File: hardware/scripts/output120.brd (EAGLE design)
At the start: 100 x 80 mm, 378 parts

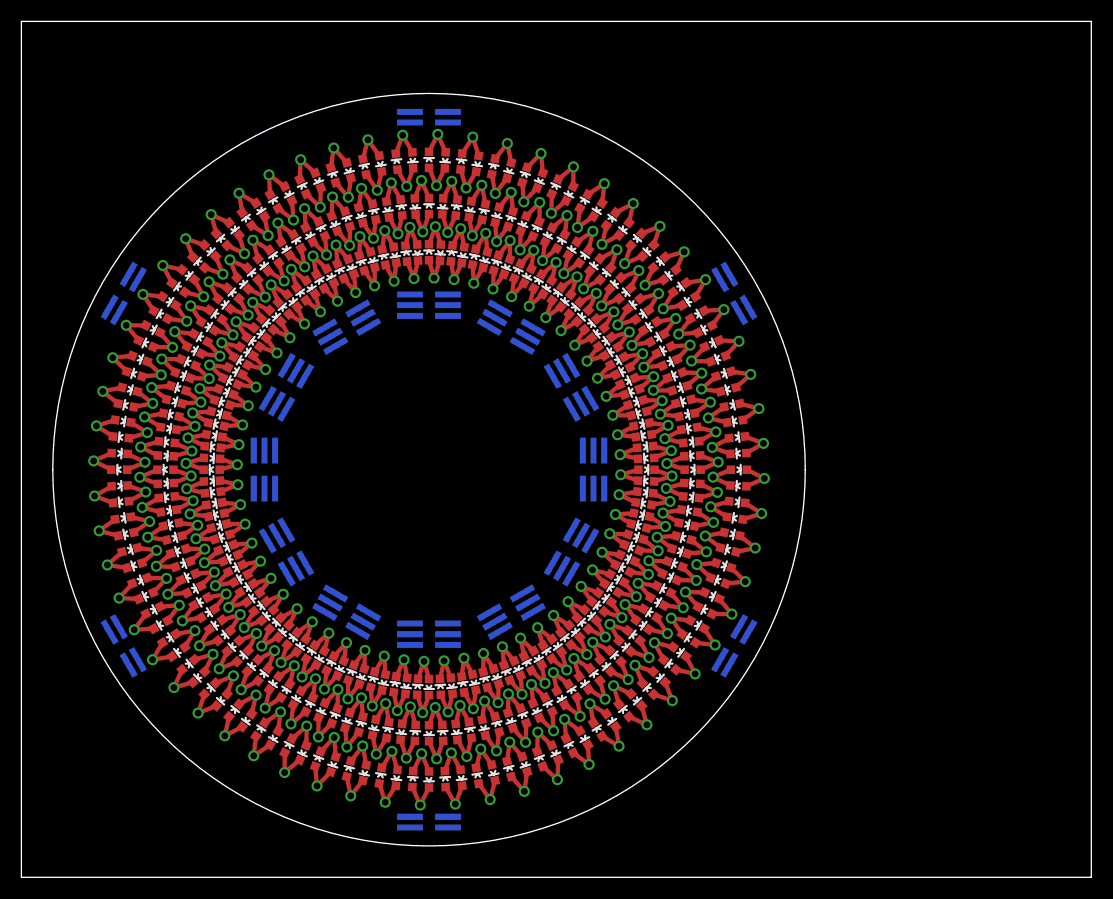
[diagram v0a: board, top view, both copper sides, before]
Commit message: More cleanup and reorganization of old attempts
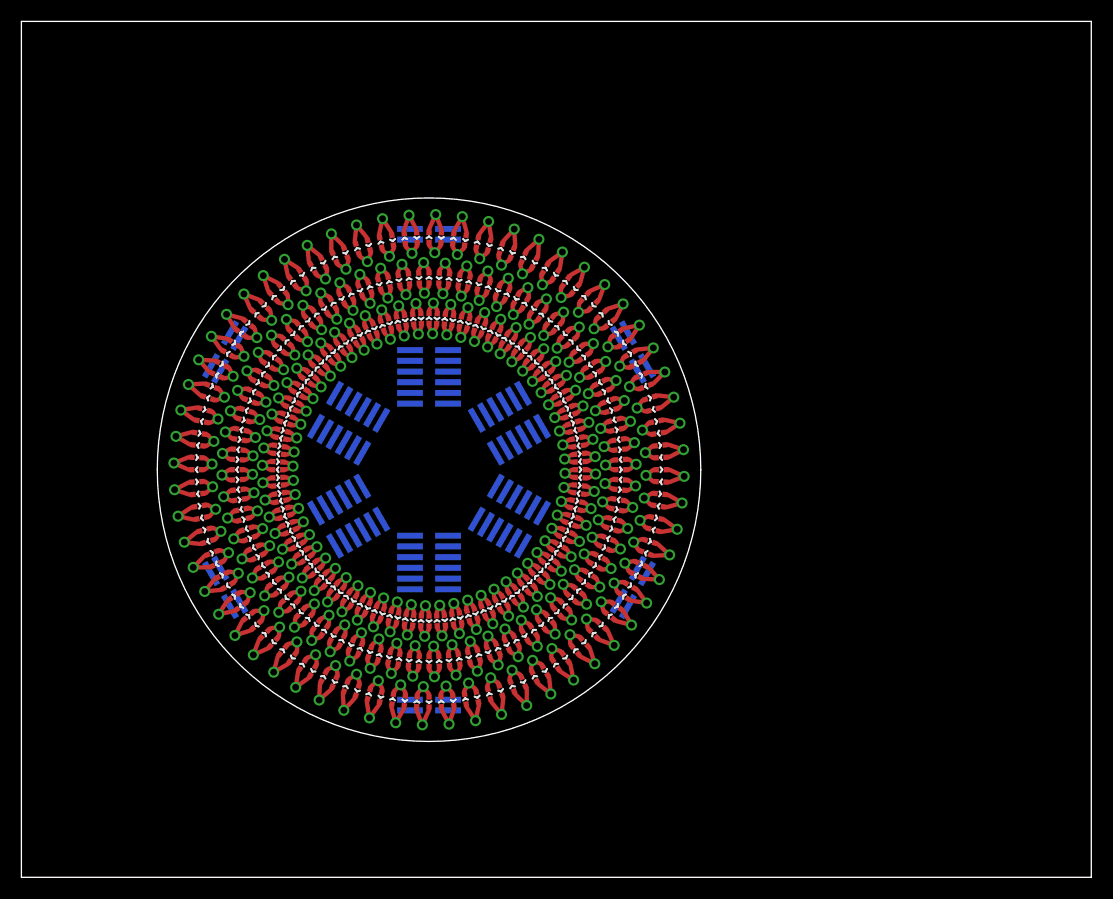
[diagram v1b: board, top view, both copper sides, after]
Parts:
- LED1, LED10, LED100, LED101, LED102, LED103, LED104, LED105, LED106, LED107, LED108, LED109, LED11, LED110, LED111, LED112, LED113, LED114, LED115, LED116, LED117, LED118, LED119, LED12, LED120, LED121, LED122, LED123, LED124, LED125, LED126, LED127, LED128, LED129, LED13, LED130, LED131, LED132, LED133, LED134, LED135, LED136, LED137, LED138, LED139, LED14, LED140, LED141, LED142, LED143, LED144, LED145, LED146, LED147, LED148, LED149, LED15, LED150, LED151, LED152, LED153, LED154, LED155, LED156, LED157, LED158, LED159, LED16, LED160, LED161, LED162, LED163, LED164, LED165, LED166, LED167, LED168, LED169, LED17, LED170, LED171, LED172, LED173, LED174, LED175, LED176, LED177, LED178, LED179, LED18, LED180, LED181, LED182, LED183, LED184, LED185, LED186, LED187, LED188, LED189, LED19, LED190, LED191, LED192, LED193, LED194, LED195, LED196, LED197, LED198, LED199, LED2, LED20, LED200, LED201, LED202, LED203, LED204, LED205, LED206, LED207, LED208, LED209, LED21, LED210, LED211, LED212, LED213, LED214, LED215, LED216, LED217, LED218, LED219, LED22, LED220, LED221, LED222, LED223, LED224, LED225, LED226, LED227, LED228, LED229, LED23, LED230, LED231, LED232, LED233, LED234, LED235, LED236, LED237, LED238, LED239, LED24, LED240, LED241, LED242, LED243, LED244, LED245, LED246, LED247, LED248, LED249, LED25, LED250, LED251, LED252, LED253, LED254, LED255, LED256, LED257, LED258, LED259, LED26, LED260, LED261, LED262, LED263, LED264, LED265, LED266, LED267, LED268, LED269, LED27, LED270, LED271, LED272, LED273, LED274, LED275, LED276, LED277, LED278, LED279, LED28, LED280, LED281, LED282, LED283, LED284, LED285, LED286, LED287, LED288, LED289, LED29, LED290, LED291, LED292, LED293, LED294, LED295, LED296, LED297, LED298, LED299, LED3, LED30, LED300, LED301, LED302, LED303, LED304, LED305, LED306, LED307, LED308, LED309, LED31, LED310, LED311, LED312, LED313, LED314, LED315, LED316, LED317, LED318, LED319, LED32, LED320, LED321, LED322, LED323, LED324, LED325, LED326, LED327, LED328, LED329, LED33, LED330, LED331, LED332, LED333, LED334, LED335, LED336, LED337, LED338, LED339, LED34, LED340, LED341, LED342, LED343, LED344, LED345, LED346, LED347, LED348, LED349, LED35, LED350, LED351, LED352, LED353, LED354, LED355, LED356, LED357, LED358, LED359, LED36, LED360, LED37, LED38, LED39, LED4, LED40, LED41, LED42, LED43, LED44, LED45, LED46, LED47, LED48, LED49, LED5, LED50, LED51, LED52, LED53, LED54, LED55, LED56, LED57, LED58, LED59, LED6, LED60, LED61, LED62, LED63, LED64, LED65, LED66, LED67, LED68, LED69, LED7, LED70, LED71, LED72, LED73, LED74, LED75, LED76, LED77, LED78, LED79, LED8, LED80, LED81, LED82, LED83, LED84, LED85, LED86, LED87, LED88, LED89, LED9, LED90, LED91, LED92, LED93, LED94, LED95, LED96, LED97, LED98, LED99: device Customs:LED-0603 -> Customs:LED-0402
- moved H6 24.7 mm to (29.3, 43.2), turned to 300 degrees
- moved H7 22.6 mm to (38.1, 45.3), turned to 0 degrees
- moved H5 22.3 mm to (29.3, 33.0), turned to 240 degrees
- moved H8 21.9 mm to (44.3, 41.7), turned to 60 degrees
- moved H9 20.0 mm to (44.3, 34.5), turned to 120 degrees
- moved H4 18.4 mm to (38.1, 27.9), turned to 180 degrees
- moved H10 17.0 mm to (38.1, 30.9), turned to 180 degrees
- moved H3 13.5 mm to (46.9, 33.0), turned to 120 degrees
- moved H11 13.3 mm to (31.9, 34.5), turned to 240 degrees
- moved H16 10.9 mm to (38.1, 16.1)
- moved H13 10.9 mm to (38.1, 60.1)
- moved H14 10.9 mm to (57.2, 49.1)
- moved H15 10.9 mm to (57.2, 27.1)
- moved H17 10.9 mm to (19.0, 27.1)
- moved H18 10.9 mm to (19.0, 49.1)
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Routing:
- net N$18: track 3.44 -> 1.53 mm
- net N$3: track 3.44 -> 1.53 mm
- net N$33: track 3.44 -> 1.53 mm
- net N$48: track 3.44 -> 1.53 mm
- net N$14: track 3.44 -> 1.53 mm
- net N$59: track 3.44 -> 1.53 mm
- net N$29: track 3.44 -> 1.53 mm
- net N$44: track 3.44 -> 1.53 mm
- net N$58: track 3.44 -> 1.53 mm
- net N$13: track 3.44 -> 1.53 mm
- net N$43: track 3.44 -> 1.53 mm
- net N$28: track 3.44 -> 1.53 mm
- net N$5: track 3.44 -> 1.53 mm
- net N$20: track 3.44 -> 1.53 mm
- net N$50: track 3.44 -> 1.53 mm
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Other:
- outline, holes or cut-outs redrawn
